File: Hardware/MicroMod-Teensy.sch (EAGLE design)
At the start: 65 parts, among them J1 MICROMOD-2222, U1 IMXRT1062DV10X10, U2 W25QXX3X2, U3 MKL02Z32VFG4, Y1 32.768kHz, Y2 24MHz

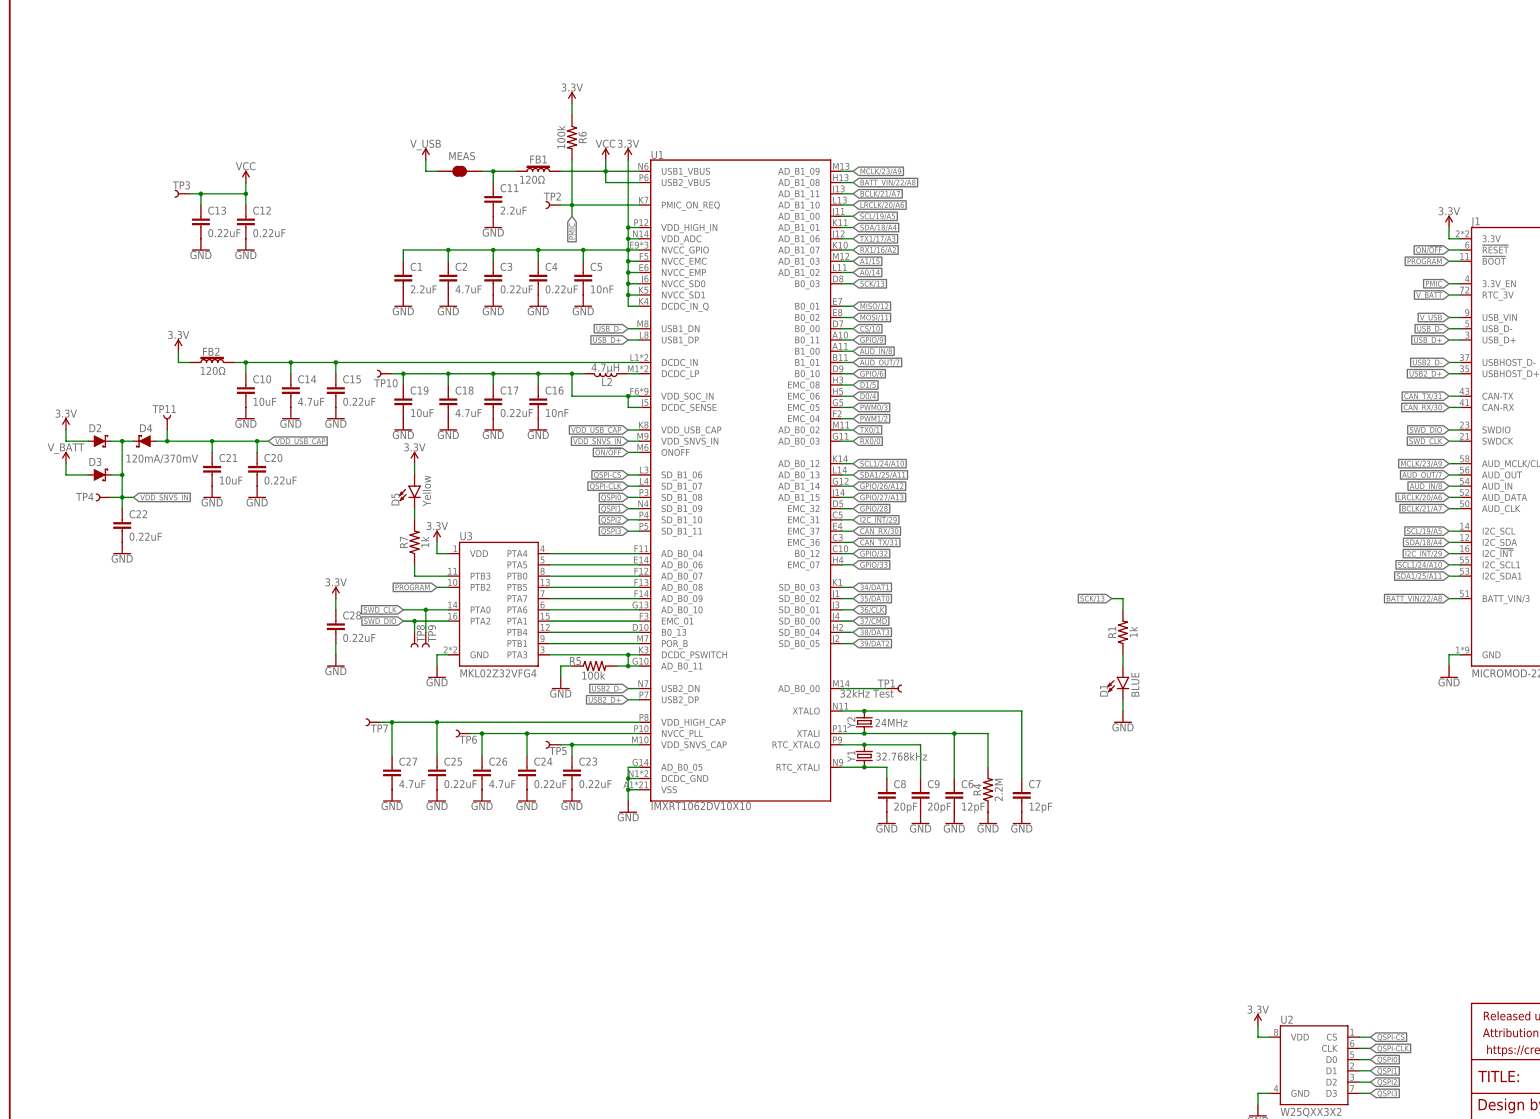
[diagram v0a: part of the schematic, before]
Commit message: Add power control circuitry.
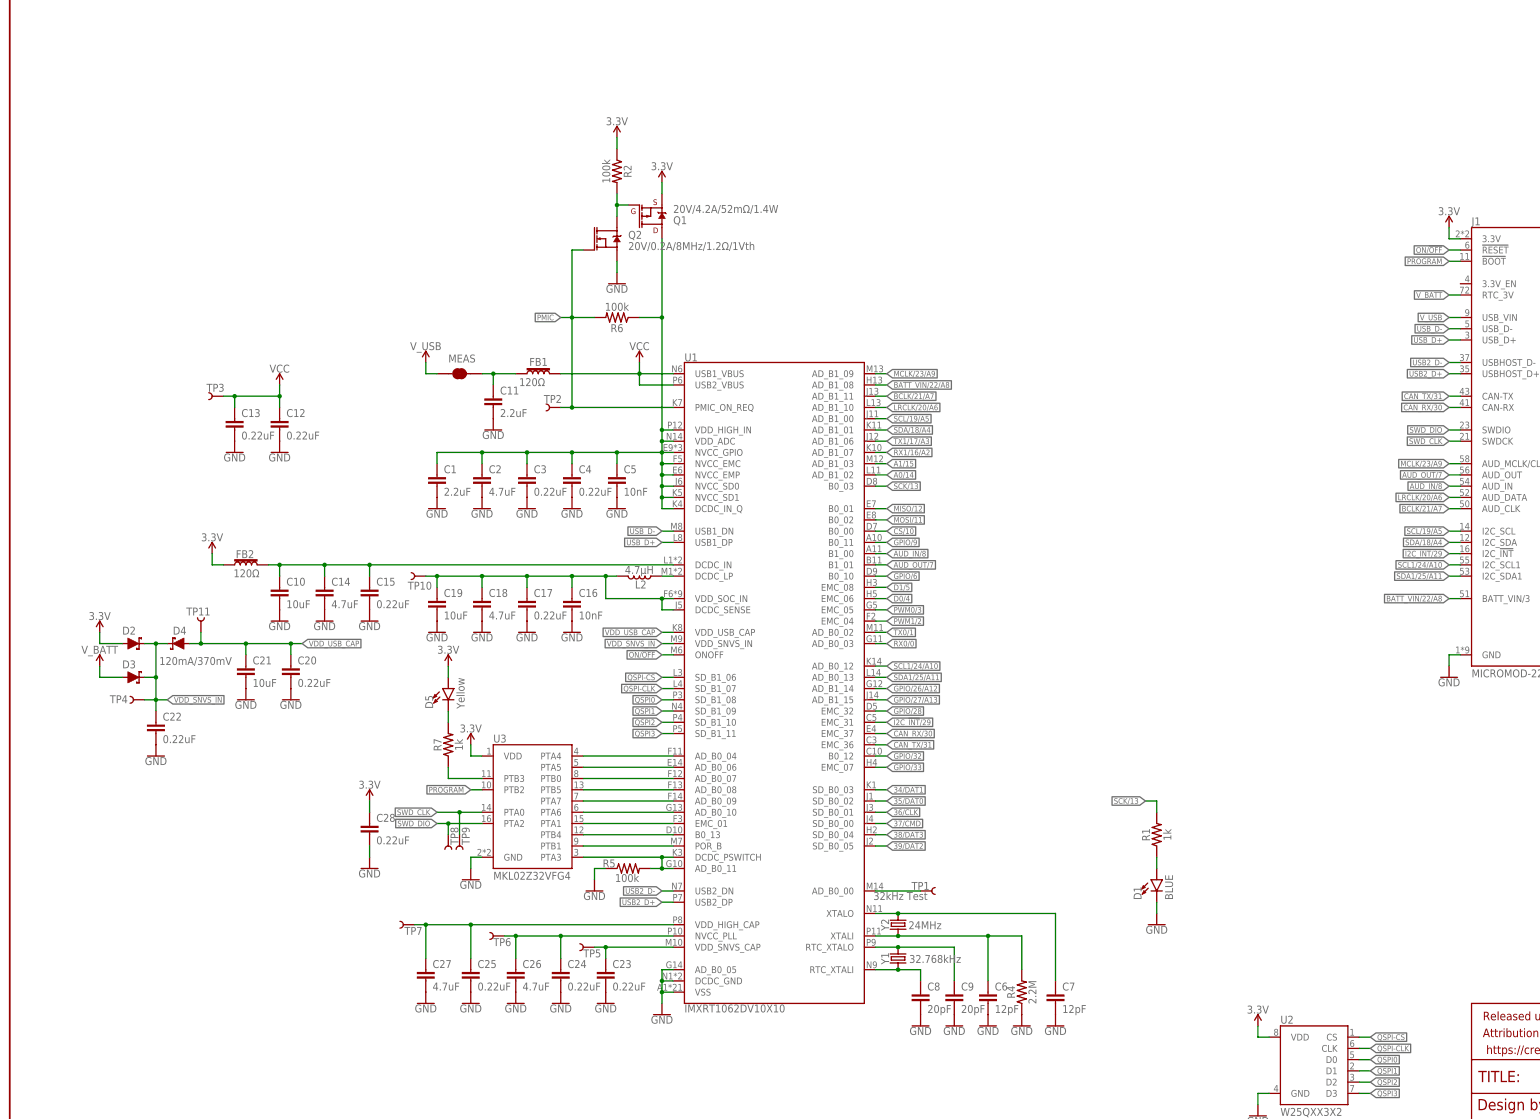
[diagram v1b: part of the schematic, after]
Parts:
- added Q1: 20V/4.2A/52mΩ/1.4W, SparkFun-DiscreteSemi:MOSFET_PCH-DMG2305UX-7
- added Q2: 20V/0.2A/8MHz/1.2Ω/1Vth, SparkFun-DiscreteSemi:MOSFET-NCH-RE1C00UNTL
- added R2: 100k, SparkFun-Resistors:100KOHM-0402T-1/16W-1%
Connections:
- new net 3.3V_CONTROLLED: C1.1, C2.1, C3.1, C4.1, C5.1, Q1.D, R6.1, U1.DCDC_IN_Q, U1.NVCC_EMC, U1.NVCC_EMP, U1.NVCC_GPIO, U1.NVCC_SD0, U1.NVCC_SD1, U1.VDD_ADC, U1.VDD_HIGH_IN
- new net N$7: Q1.G, Q2.D, R2.2
- net 3.3V: now also Q1.S, R2.1; no longer C1.1, C2.1, C3.1, C4.1, C5.1, R6.1, U1.DCDC_IN_Q, U1.NVCC_EMC, U1.NVCC_EMP, U1.NVCC_GPIO, U1.NVCC_SD0, U1.NVCC_SD1, U1.VDD_ADC, U1.VDD_HIGH_IN
- net GND: now also Q2.S
- net PMIC: now also Q2.G; no longer J1.3.3V_EN
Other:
- moved on the sheet: C1, C10, C11, C12, C13, C14, C15, C16, C17, C18, C19, C2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

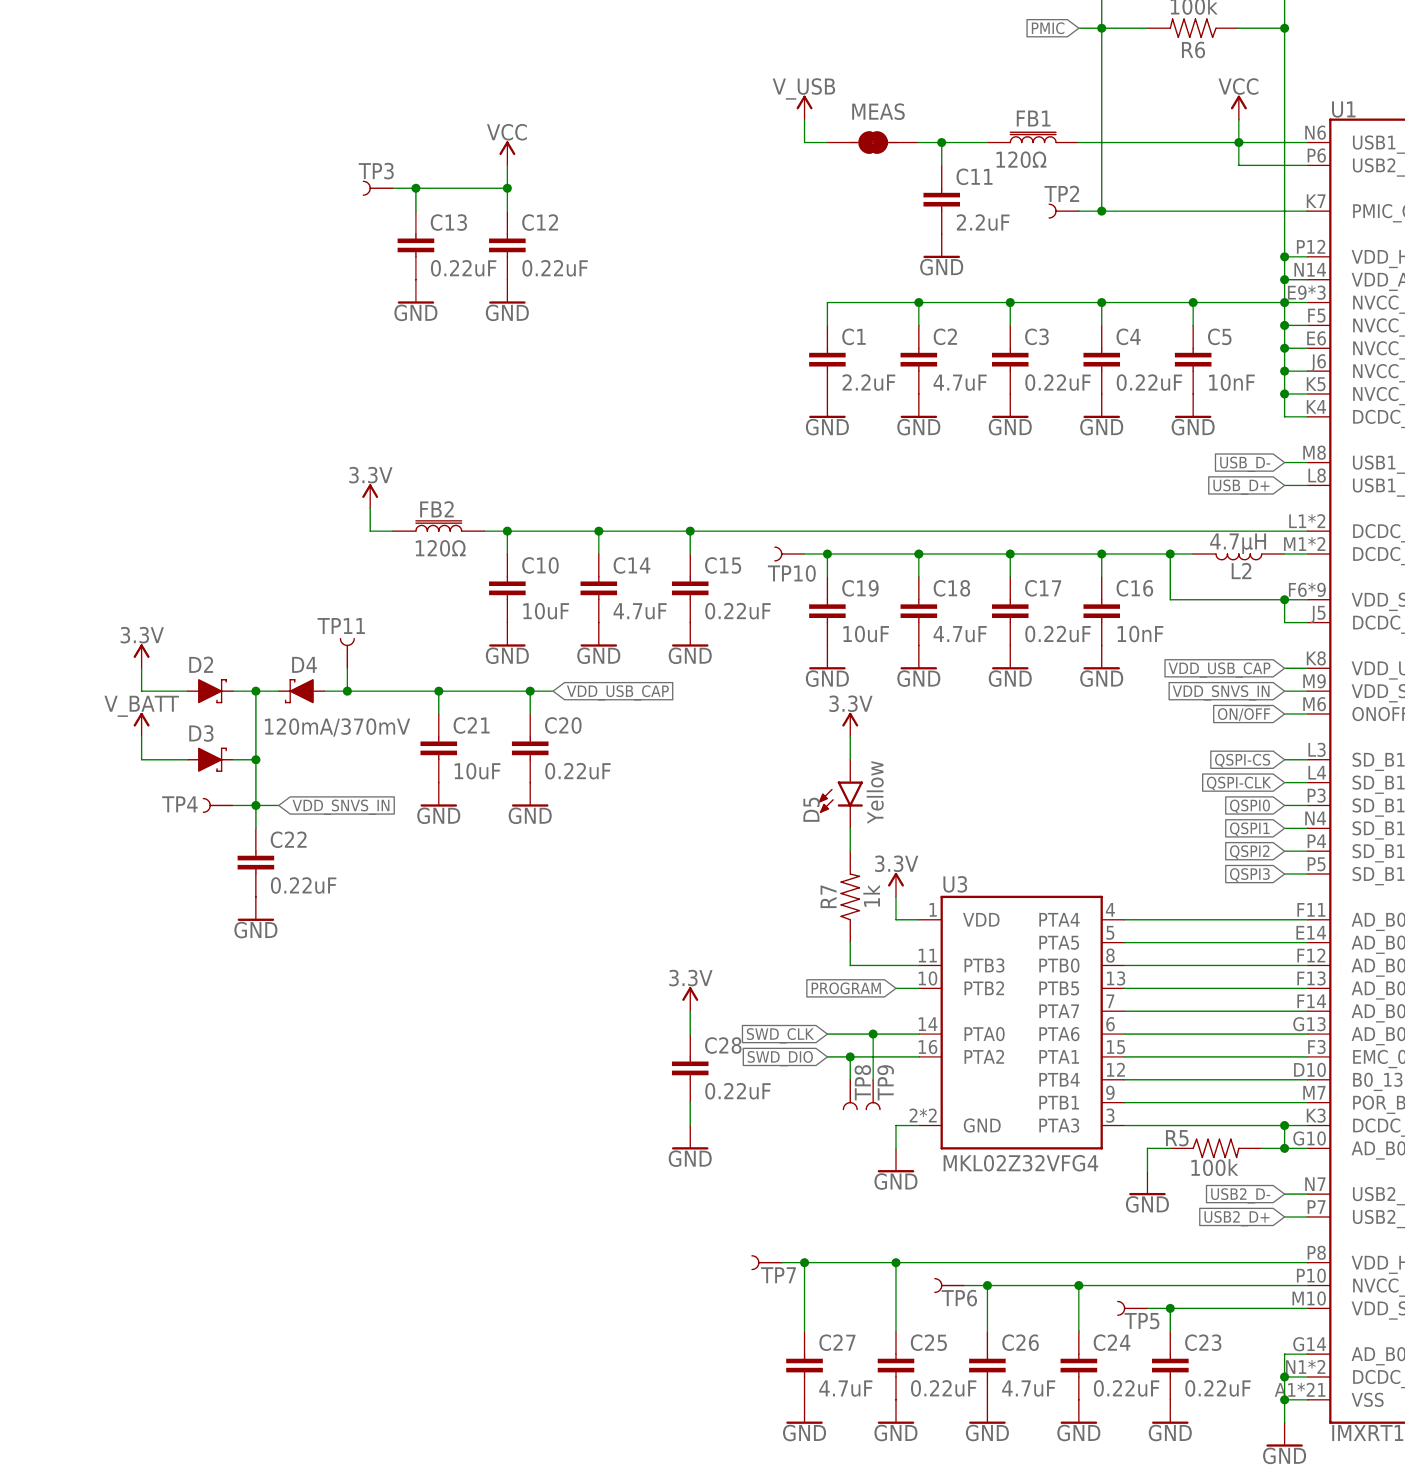
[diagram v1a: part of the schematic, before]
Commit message: Remove cream from test points
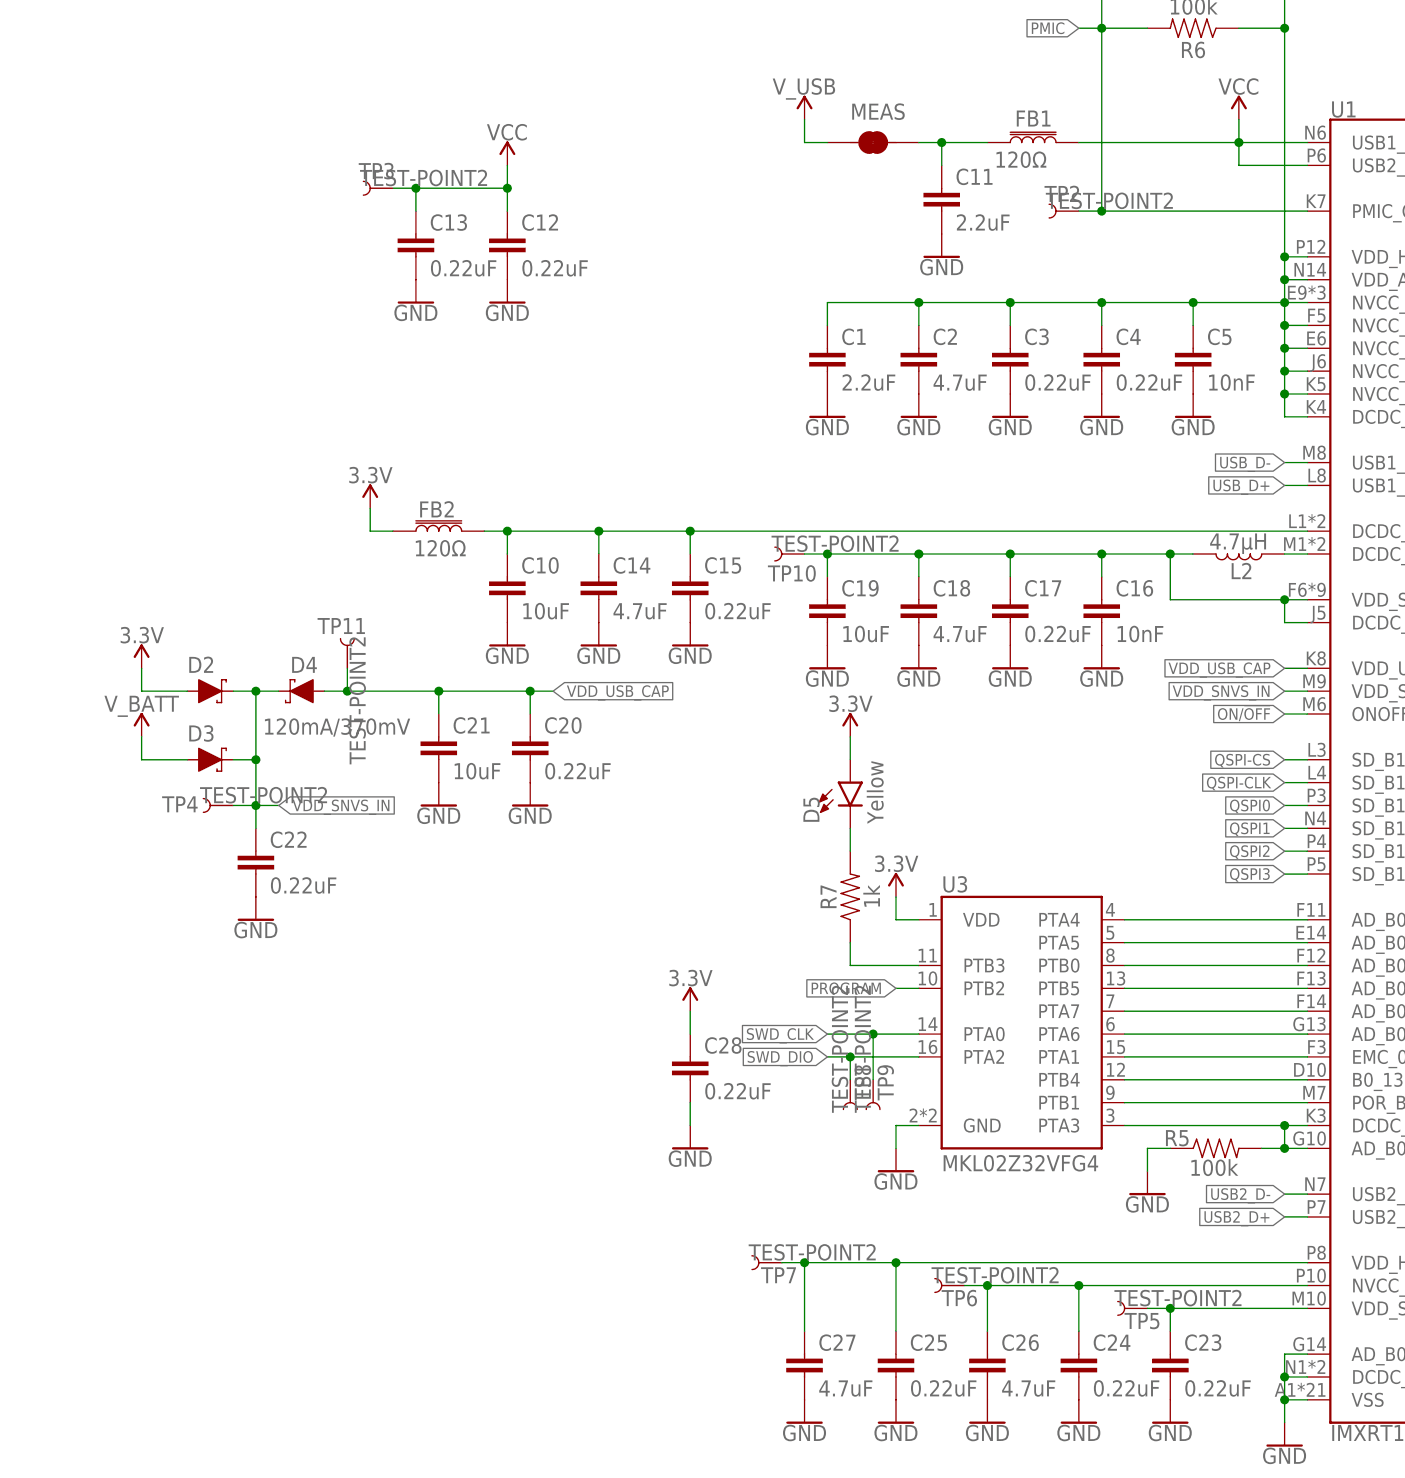
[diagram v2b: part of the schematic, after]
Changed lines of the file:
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@@
 <part name="GND21" library="SparkFun-PowerSymbols" deviceset="GND" device=""/>
 <part name="GND22" library="SparkFun-PowerSymbols" deviceset="GND" device=""/>
-<part name="TP3" library="SparkFun-Connectors" deviceset="TEST-POINT" device="2" value=""/>
+<part name="TP3" library="SparkFun-Connectors" deviceset="TEST-POINT" device="2" value="TEST-POINT2"/>
 <part name="SUPPLY10" library="SparkFun-PowerSymbols" deviceset="3.3V" device=""/>
 <part name="C14" library="SparkFun-Capacitors" deviceset="4.7UF" device="-0402_TIGHT-6.3V-20%-X5R" value="4.7uF"/>
@@
 <part name="C22" library="SparkFun-Capacitors" deviceset="0.22UF" device="-0402T-10V-10%" value="0.22uF"/>
 <part name="GND35" library="SparkFun-PowerSymbols" deviceset="GND" device=""/>
-<part name="TP4" library="SparkFun-Connectors" deviceset="TEST-POINT" device="2" value=""/>
+<part name="TP4" library="SparkFun-Connectors" deviceset="TEST-POINT" device="2" value="TEST-POINT2"/>
 <part name="SUPPLY16" library="SparkFun-PowerSymbols" deviceset="V_BATT" device=""/>
 <part name="SUPPLY17" library="SparkFun-PowerSymbols" deviceset="3.3V" device=""/>
@@
 <part name="C27" library="SparkFun-Capacitors" deviceset="4.7UF" device="-0402_TIGHT-6.3V-20%-X5R" value="4.7uF"/>
 <part name="GND40" library="SparkFun-PowerSymbols" deviceset="GND" device=""/>
-<part name="TP5" library="SparkFun-Connectors" deviceset="TEST-POINT" device="2" value=""/>
-<part name="TP6" library="SparkFun-Connectors" deviceset="TEST-POINT" device="2" value=""/>
-<part name="TP7" library="SparkFun-Connectors" deviceset="TEST-POINT" device="2" value=""/>
+<part name="TP5" library="SparkFun-Connectors" deviceset="TEST-POINT" device="2" value="TEST-POINT2"/>
+<part name="TP6" library="SparkFun-Connectors" deviceset="TEST-POINT" device="2" value="TEST-POINT2"/>
+<part name="TP7" library="SparkFun-Connectors" deviceset="TEST-POINT" device="2" value="TEST-POINT2"/>
 <part name="FD1" library="SparkFun-Aesthetics" deviceset="FIDUCIAL" device="UFIDUCIAL"/>
 <part name="FD2" library="SparkFun-Aesthetics" deviceset="FIDUCIAL" device="UFIDUCIAL"/>
@@
 <part name="D5" library="SparkFun-LED" deviceset="LED-YELLOW" device="0603" value="Yellow"/>
 <part name="SUPPLY19" library="SparkFun-PowerSymbols" deviceset="3.3V" device=""/>
-<part name="TP8" library="SparkFun-Connectors" deviceset="TEST-POINT" device="2" value=""/>
-<part name="TP9" library="SparkFun-Connectors" deviceset="TEST-POINT" device="2" value=""/>
+<part name="TP8" library="SparkFun-Connectors" deviceset="TEST-POINT" device="2" value="TEST-POINT2"/>
+<part name="TP9" library="SparkFun-Connectors" deviceset="TEST-POINT" device="2" value="TEST-POINT2"/>
 <part name="C28" library="SparkFun-Capacitors" deviceset="0.22UF" device="-0402T-10V-10%" value="0.22uF"/>
 <part name="SUPPLY20" library="SparkFun-PowerSymbols" deviceset="3.3V" device=""/>
 <part name="GND43" library="SparkFun-PowerSymbols" deviceset="GND" device=""/>
-<part name="TP10" library="SparkFun-Connectors" deviceset="TEST-POINT" device="2" value=""/>
-<part name="TP11" library="SparkFun-Connectors" deviceset="TEST-POINT" device="2" value=""/>
+<part name="TP10" library="SparkFun-Connectors" deviceset="TEST-POINT" device="2" value="TEST-POINT2"/>
+<part name="TP11" library="SparkFun-Connectors" deviceset="TEST-POINT" device="2" value="TEST-POINT2"/>
 <part name="SUPPLY6" library="SparkFun-PowerSymbols" deviceset="3.3V" device=""/>
 <part name="GND8" library="SparkFun-PowerSymbols" deviceset="GND" device=""/>
 <part name="L2" library="SparkFun-Coils" deviceset="4.7μH_SHIELDED_INDUCTOR" device="" value="4.7μH"/>
 <part name="J1" library="Teensy" deviceset="MICROMOD" device="-2222"/>
-<part name="TP2" library="SparkFun-Connectors" deviceset="TEST-POINT" device="2" value=""/>
+<part name="TP2" library="SparkFun-Connectors" deviceset="TEST-POINT" device="2" value="TEST-POINT2"/>
 <part name="Q1" library="SparkFun-DiscreteSemi" deviceset="MOSFET_PCH" device="-DMG2305UX-7" value="20V/4.2A/52mΩ/1.4W"/>
 <part name="Q2" library="SparkFun-DiscreteSemi" deviceset="MOSFET-NCH" device="-RE1C00UNTL" value="20V/0.2A/8MHz/1.2Ω/1Vth"/>
